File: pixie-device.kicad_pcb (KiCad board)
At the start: 4 copper layers, 70 x 70 mm, 75 parts, among them U1 USBLC6-2SC6, U2 SPX3819M5-L-3-3, U3 W25Q128JVS, U4 ESP32-C3, U5 SN74LVC1T45DBV, Y1 40Mhz

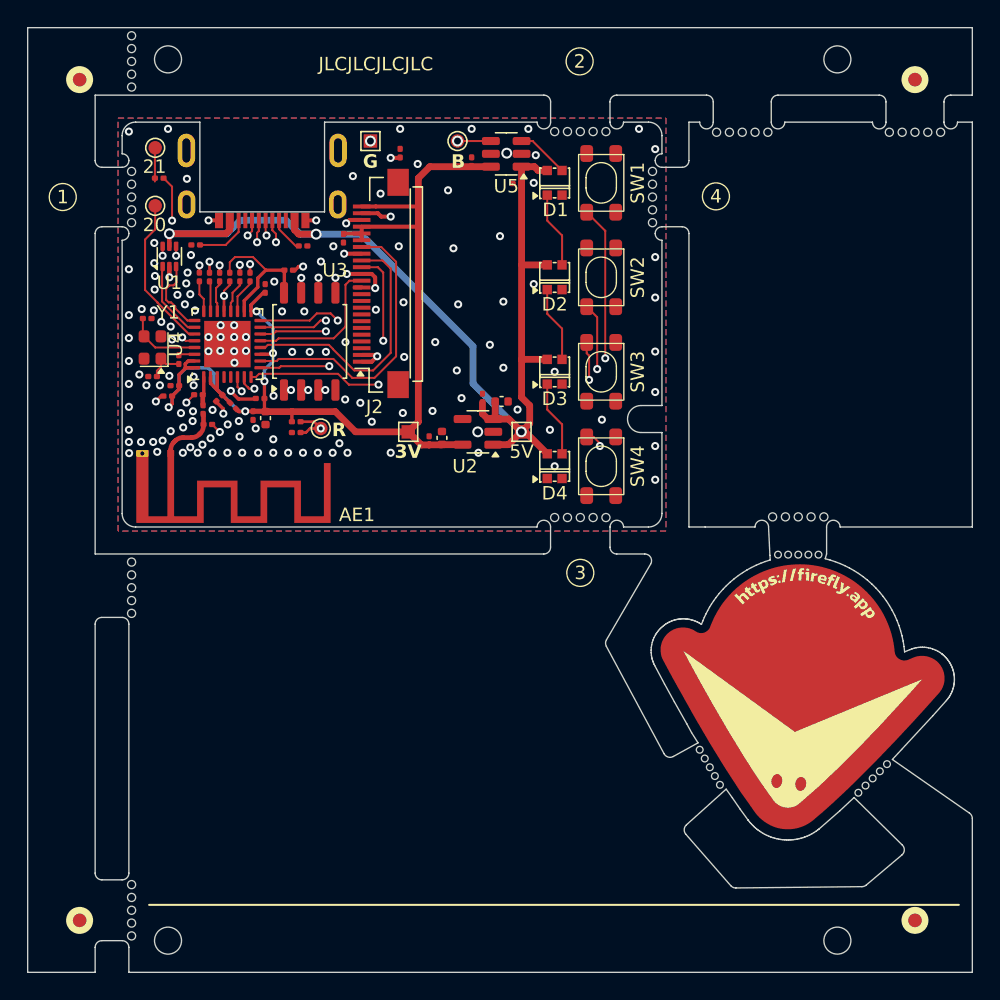
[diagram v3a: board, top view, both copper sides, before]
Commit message: Added panelization using KiKit.
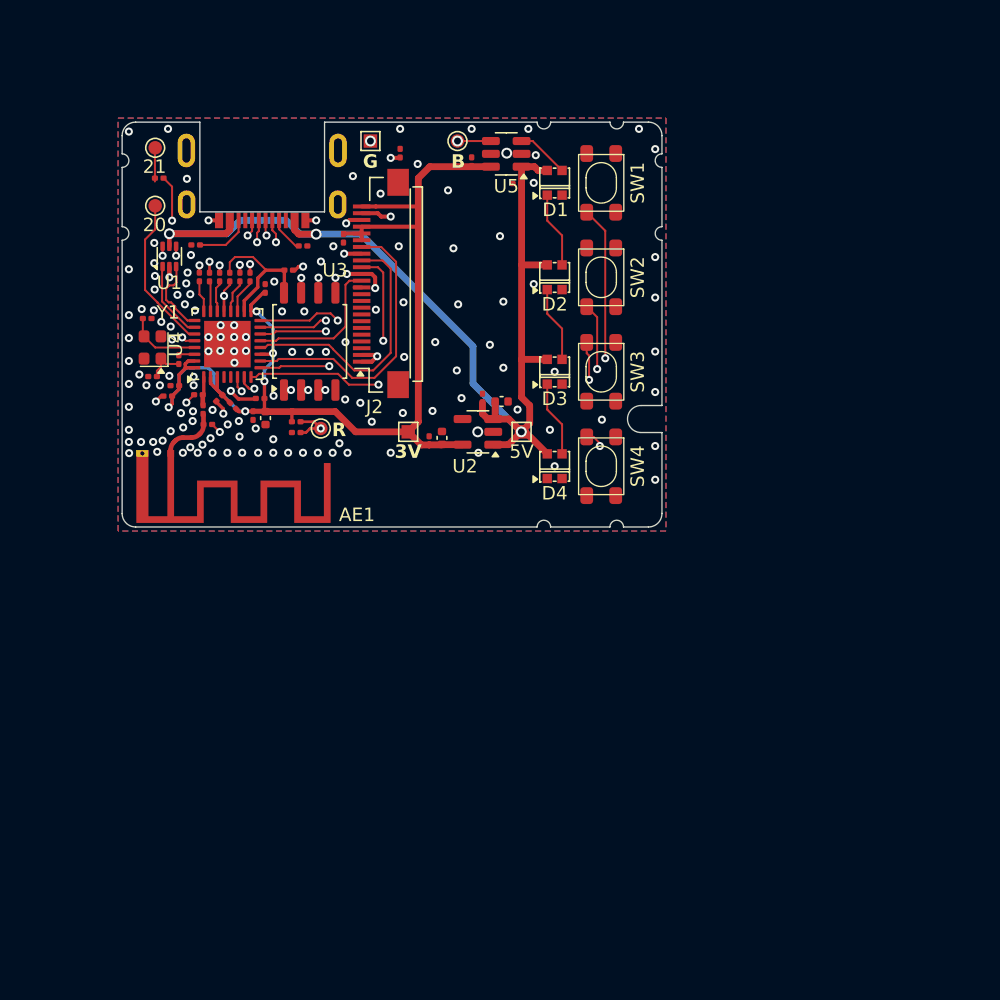
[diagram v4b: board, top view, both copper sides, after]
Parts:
- removed the REF** at (100.7, 65.5)
- removed the REF** at (139.3, 75.5)
- removed the REF** at (100.7, 75.5)
- removed the REF** at (96.8, 129.2)
- removed the REF** at (158.8, 70.8)
- removed the REF** at (158.8, 129.2)
- removed the REF** at (96.8, 66.8)
- removed the REF** at (150.1, 99.2)
- removed the REF** at (100.7, 128.4)
- removed the REF** at (100.7, 104.5)
- removed the REF** at (145.9, 70.8)
- removed the REF** at (133.9, 70.7)
- removed the REF** at (158.8, 66.8)
- removed the REF** at (133.9, 99.3)
- removed the REF** at (149.5, 113.5)
- added REF**: Tab, kikit:Tab, F.Cu at (140.2, 75.5)
- added REF**: Tab, kikit:Tab, F.Cu at (133.9, 69.8)
- added REF**: Tab, kikit:Tab, F.Cu at (99.8, 75.5)
- added REF**: Tab, kikit:Tab, F.Cu at (133.9, 100.2)
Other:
- board size 70 x 70 mm -> 40 x 30 mm
- board text removed: "1"
- board text removed: "2"
- board text removed: "3"
- board text removed: "4"
- board text removed: "JLCJLCJLCJLC"

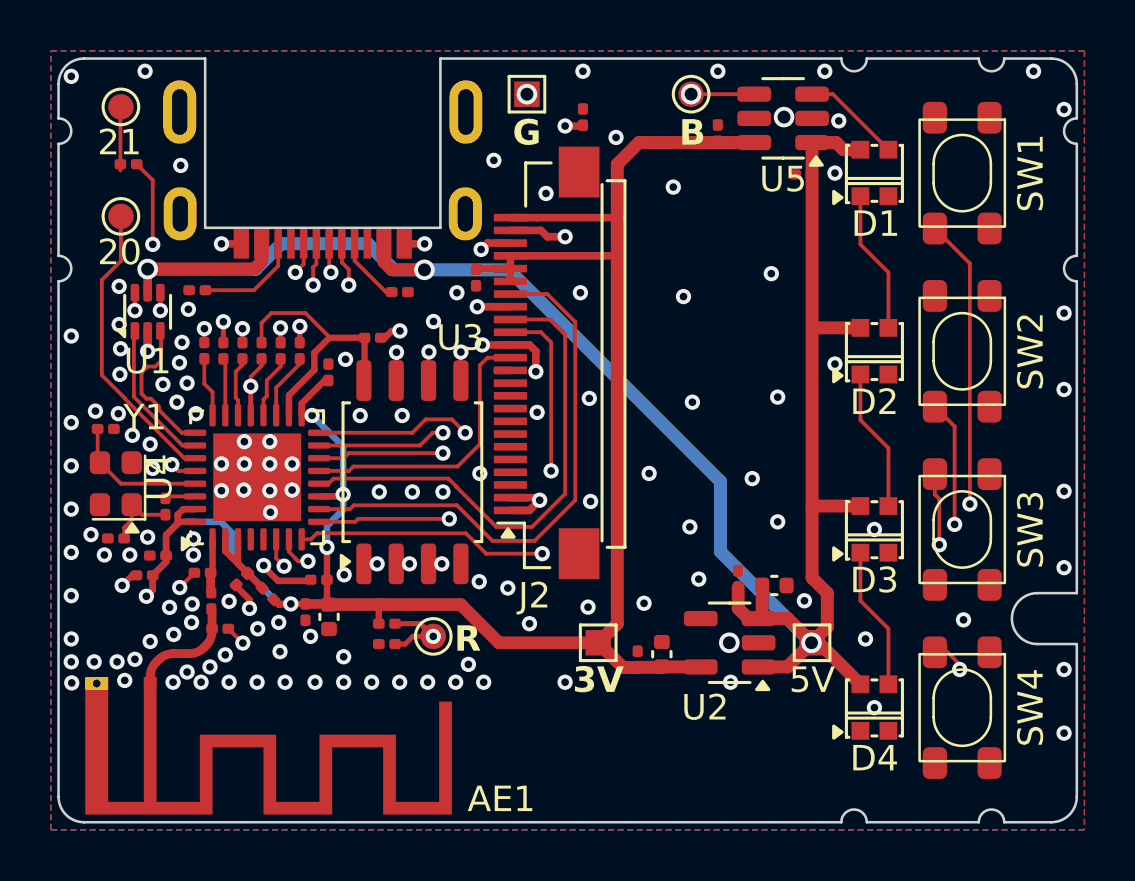
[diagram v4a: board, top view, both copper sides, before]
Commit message: Nove mouse bite tabs for better panel strength.
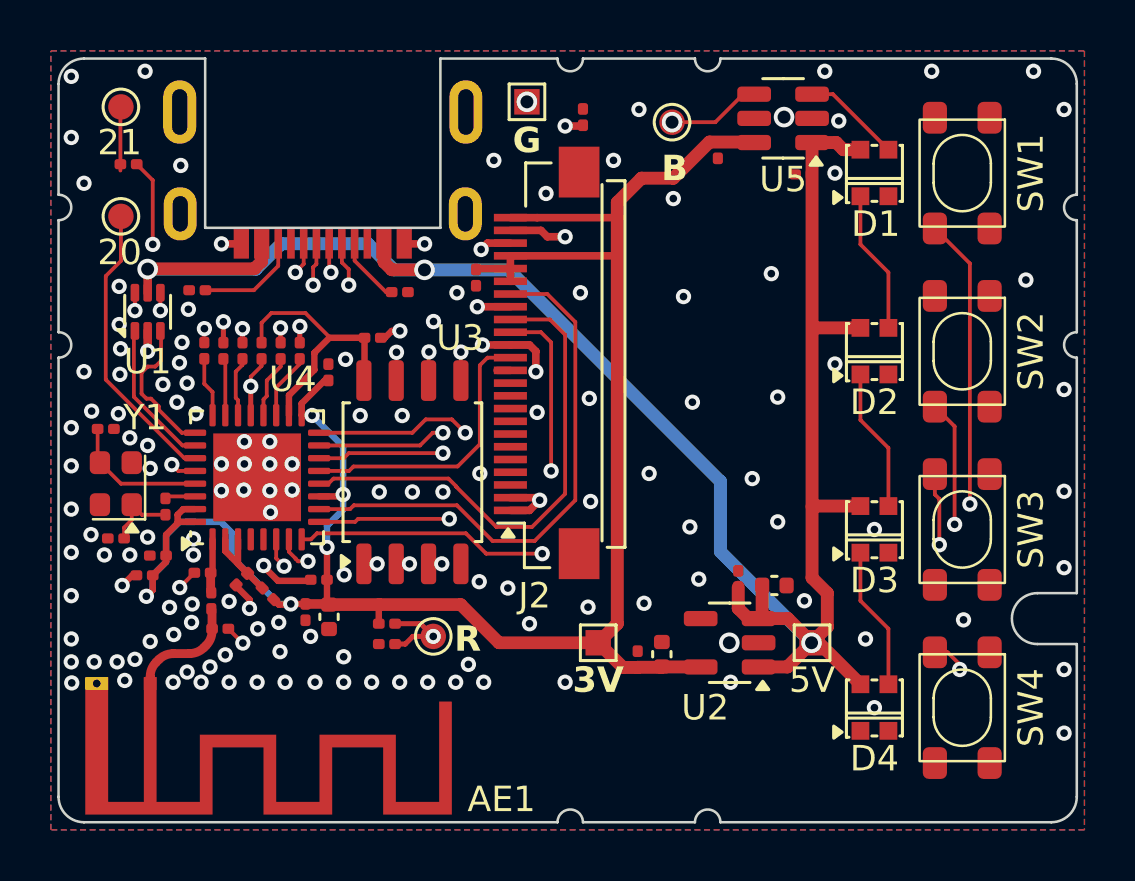
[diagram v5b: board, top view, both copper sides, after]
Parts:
- moved REF** 11.1 mm to (122.8, 69.8)
- moved REF** 11.1 mm to (122.8, 100.2)
- moved REF** 3.00 mm to (140.2, 78.5)
- moved REF** 3.00 mm to (99.8, 78.5)
- moved BOOT1 1.33 mm to (124.1, 72.5)
- moved C19 0.67 mm to (125.9, 73.6), turned to -90 degrees
- moved GND1 0.30 mm to (118.4, 71.7)
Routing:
- net 3V3: track 80.7 -> 79.8 mm
- net GND: vias 146 -> 148
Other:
- outline, holes or cut-outs redrawn

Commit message: Move buttons and LEDs 2mm right to accomodate thumb space between the screen.
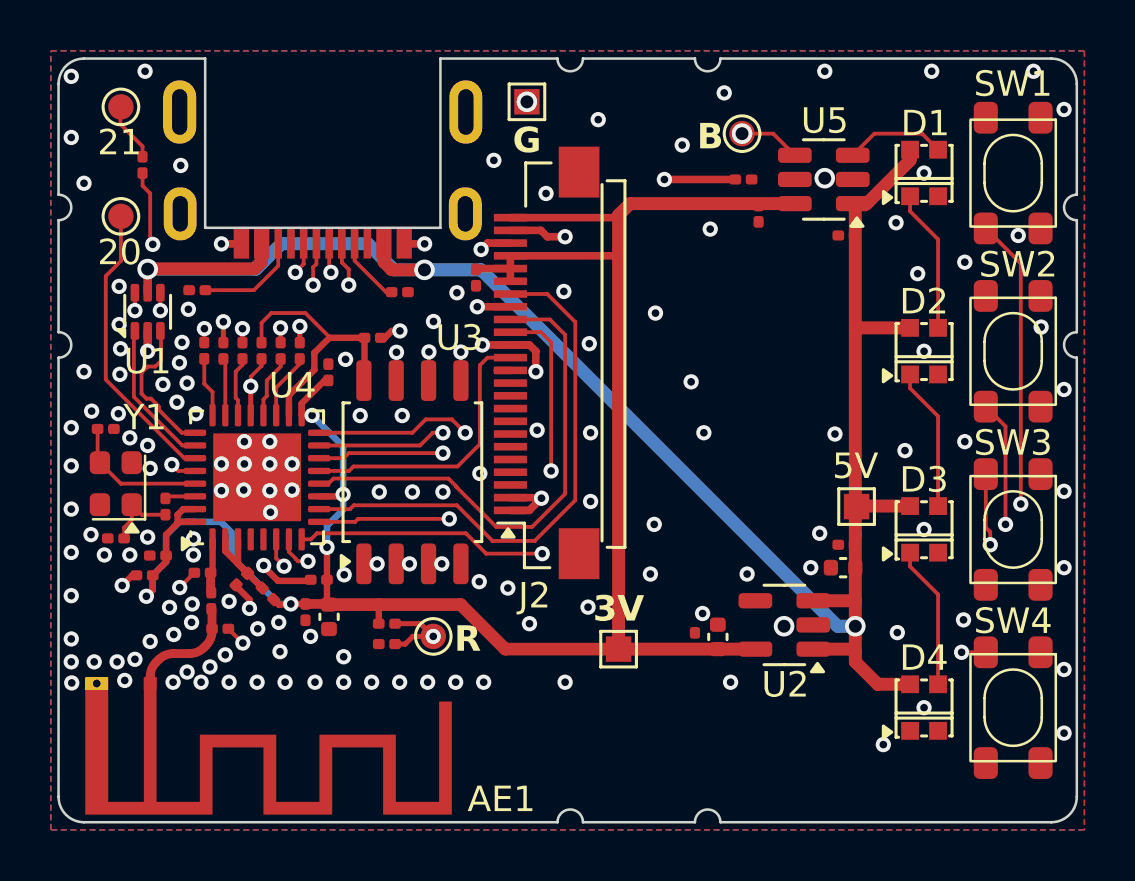
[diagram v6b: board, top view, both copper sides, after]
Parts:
- moved R12 6.76 mm to (126.9, 74.8), turned to 0 degrees
- moved 5V1 5.63 mm to (131.3, 87.6)
- moved REF** 5.46 mm to (128.4, 87.2)
- moved REF** 5.46 mm to (128.1, 80.2)
- moved C2 4.46 mm to (130.9, 89.1), turned to 180 degrees
- moved C19 2.96 mm to (127.5, 76.1)
- moved C20 2.94 mm to (130.9, 77.0)
- moved U5 2.88 mm to (130.1, 74.8)
- moved C1 2.79 mm to (130.8, 90.0), turned to 180 degrees
- moved BOOT1 2.79 mm to (126.8, 73.0)
- moved C3 2.36 mm to (125.0, 92.9)
- moved C4 2.30 mm to (125.9, 92.7)
- moved U2 2.26 mm to (128.5, 92.2)
- moved SW1 2.00 mm to (137.5, 74.5)
- moved SW2 2.00 mm to (137.5, 81.5)
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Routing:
- net 5V: track 79.9 -> 74.7 mm
- net /MCU/SW_1: track 38.6 -> 41.2 mm
- net Net-(J2-LEDK): track 7.32 -> 9.87 mm
- net 3V3: track 79.8 -> 81.9 mm
- net /PIXEL: track 26.2 -> 24.1 mm
- net /SW_3: track 28.5 -> 30.5 mm
- net /MCU/SW_2: track 31.2 -> 33.2 mm
- net /SW_4: track 30.8 -> 30.2 mm
- net GND: track 17.6 -> 17.8 mm, vias 148 -> 154
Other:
- outline, holes or cut-outs redrawn
